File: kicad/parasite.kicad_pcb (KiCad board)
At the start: 2 copper layers, 22 x 126.4 mm, 33 parts, among them Q1 MMBT3904, Q2 MMBT3904, Q3 AO3407, Q4 Q_Photo_NPN, U1 E73-2G4M08S1C-52840, U2 SHTC3, Y1 32.768kHz

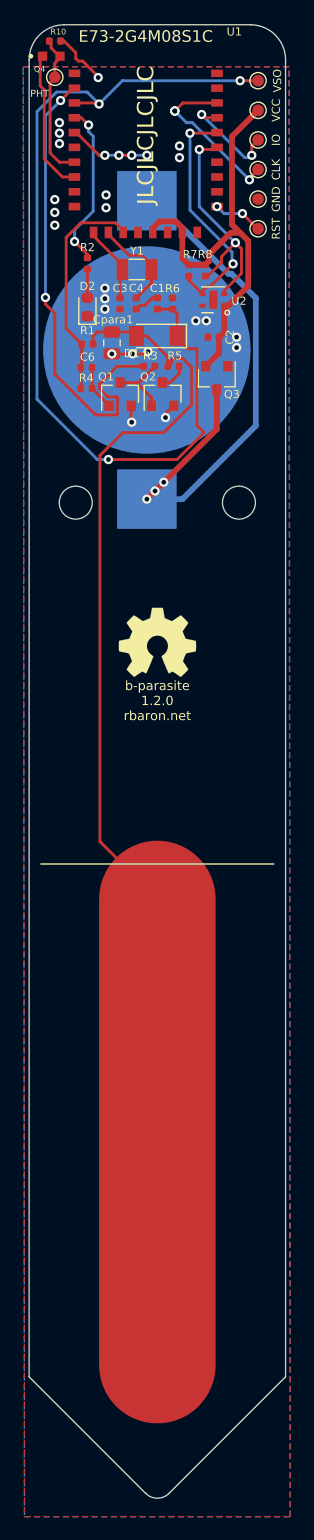
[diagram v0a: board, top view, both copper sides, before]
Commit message: using larger footprint for easier soldering
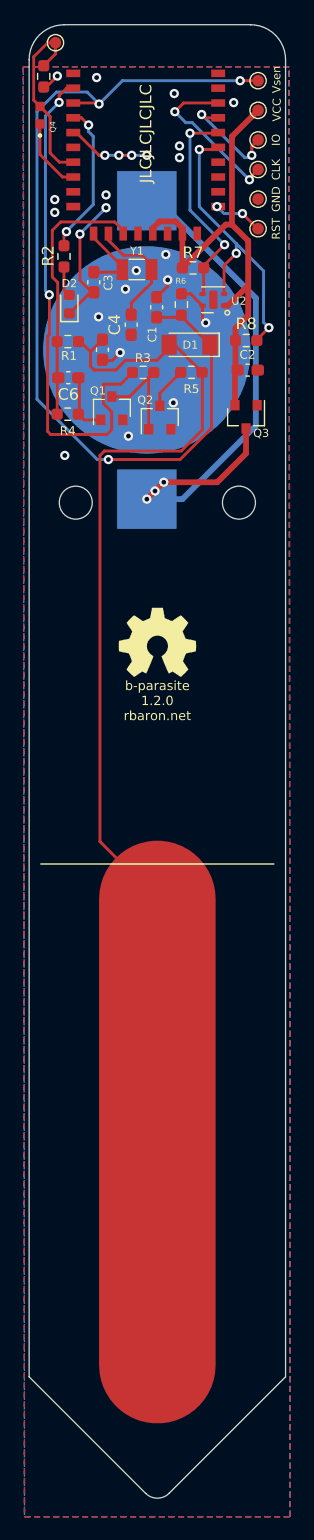
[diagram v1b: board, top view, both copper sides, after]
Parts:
- C1, C2, C3, C4, C6: footprint Capacitor_SMD:C_0402_1005Metric -> Capacitor_SMD:C_0603_1608Metric_Pad1.08x0.95mm_HandSolder
- Cpara1: footprint Capacitor_SMD:C_0805_2012Metric -> Capacitor_SMD:C_0603_1608Metric_Pad1.08x0.95mm_HandSolder
- R1, R10, R2, R3, R4, R5, R6, R7, R8: footprint Resistor_SMD:R_0402_1005Metric -> Resistor_SMD:R_0603_1608Metric_Pad0.98x0.95mm_HandSolder
- TP4: value VSO -> Vsen
- moved R8 6.96 mm to (75.6, 54.1), turned to 0 degrees
- moved Q4 5.15 mm to (57.9, 34.8), turned to 90 degrees
- moved Q3 4.18 mm to (75.6, 60.6)
- moved C2 4.08 mm to (75.8, 56.6), turned to 0 degrees
- moved R10 3.18 mm to (58.2, 31.4), turned to 90 degrees
- moved TP3 2.96 mm to (59.3, 28.5)
- moved D1 2.91 mm to (70.8, 54.5)
- moved C3 2.90 mm to (62.5, 49.1)
- moved R4 2.73 mm to (60.3, 60.4)
- moved R2 2.10 mm to (60.0, 46.9)
- moved Q2 2.00 mm to (68.2, 60.7)
- moved C4 1.87 mm to (65.8, 52.7)
- moved C6 1.79 mm to (60.4, 57.3)
- moved R1 1.69 mm to (60.3, 54.2)
- moved R5 1.62 mm to (70.9, 56.8), turned to 180 degrees
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- renumbered PHT to TP3
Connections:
- U1 pad 1: Net-(U1-Pad1) -> unconnected-(U1-Pad1)
- U1 pad 10: Net-(U1-Pad10) -> unconnected-(U1-Pad10)
- U1 pad 17: Net-(U1-Pad17) -> unconnected-(U1-Pad17)
- U1 pad 25: Net-(U1-Pad25) -> unconnected-(U1-Pad25)
- U1 pad 27: Net-(U1-Pad27) -> unconnected-(U1-Pad27)
- U1 pad 29: Net-(U1-Pad29) -> unconnected-(U1-Pad29)
- U1 pad 31: Net-(U1-Pad31) -> unconnected-(U1-Pad31)
- U1 pad 41: Net-(U1-Pad41) -> unconnected-(U1-Pad41)
- U1 pad 43: Net-(U1-Pad43) -> unconnected-(U1-Pad43)
- U1 pad 6: Net-(U1-Pad6) -> unconnected-(U1-Pad6)
- U1 pad 9: Net-(U1-Pad9) -> unconnected-(U1-Pad9)
- U2 pad 5: Net-(U2-Pad5) -> unconnected-(U2-Pad5)
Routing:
- net GND: track 20.4 -> 28.1 mm, vias 27 -> 25
- net /PHOTO_V: track 12.4 -> 6.37 mm
- net /Csen+: track 104.6 -> 110.6 mm
- net /SCL: track 20.2 -> 25.6 mm, vias 2 -> 3
- net +3V0: track 37.8 -> 42.7 mm
- net Net-(Q1-Pad3): track 6.03 -> 9.49 mm
- net /PWM: track 19.4 -> 22.8 mm
- net /PHOTO_OUT: track 12.6 -> 16.0 mm
- net /FAST_DISCH_EN: track 40.9 -> 44.0 mm
- net /SDA: track 20.9 -> 18.2 mm
- net Net-(C4-Pad2): track 8.33 -> 10.1 mm
- net Net-(C6-Pad1): track 3.90 -> 5.30 mm
- net Net-(Q2-Pad3): track 2.37 -> 3.61 mm
- net /LED: track 14.2 -> 13.0 mm
- net Net-(TP2-Pad1): track 14.5 -> 13.9 mm, vias 3 -> 2
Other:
- net class Default removed
